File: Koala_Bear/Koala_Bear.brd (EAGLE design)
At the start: 59.3 x 40 mm, 28 parts

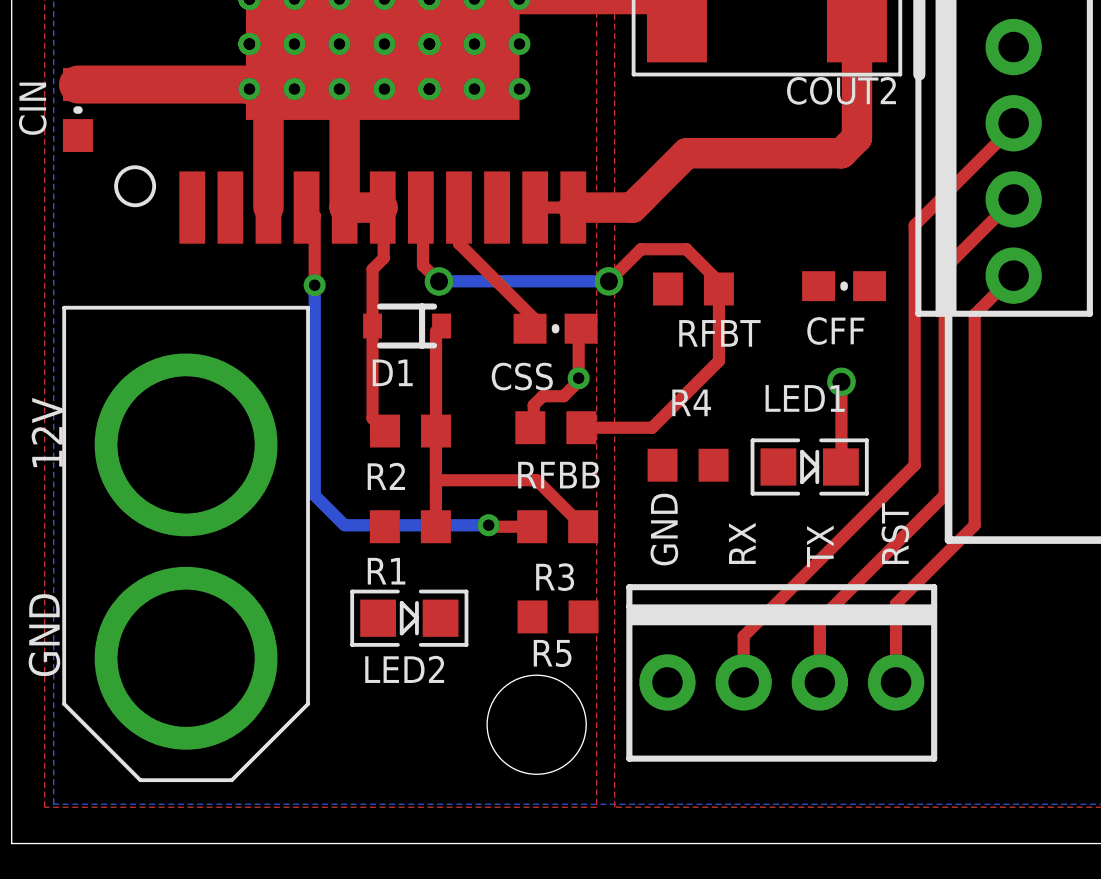
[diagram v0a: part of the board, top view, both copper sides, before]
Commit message: Rerouting completed
Koala should be successfully rerouted for RevB pending review.
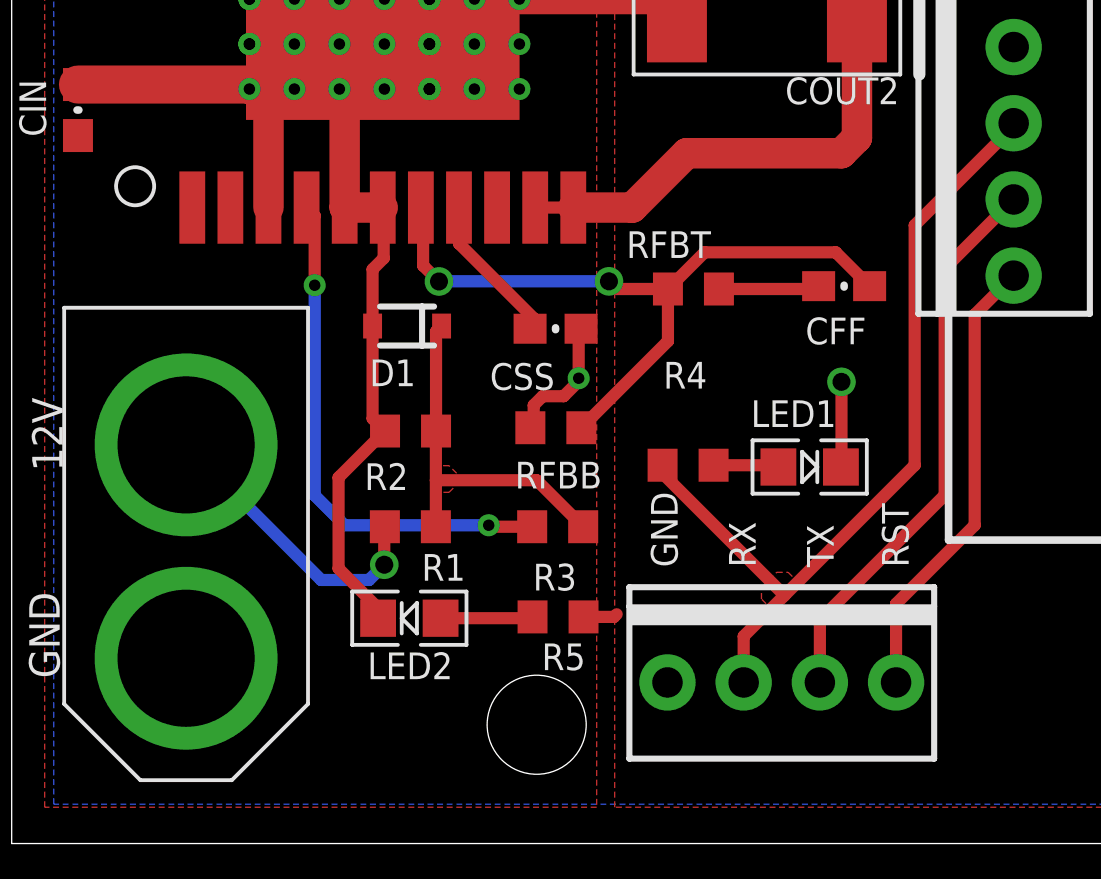
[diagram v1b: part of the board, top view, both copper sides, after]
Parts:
- turned LED2 to 180 degrees
- turned R4 to 180 degrees
- turned R5 to 0 degrees
- turned RFBT to 0 degrees
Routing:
- net VIN: track 0.00 -> 9.97 mm, vias 0 -> 1
- net GND: track 54.5 -> 61.9 mm
- net RX: track 22.4 -> 28.4 mm
- net VOUT: track 16.3 -> 20.2 mm
- net N$5: track 0.00 -> 3.08 mm
- net FB: track 21.2 -> 24.0 mm
- net N$1: track 0.00 -> 2.19 mm
- added copper zone on layer 1, net DIODE
- added copper zone on layer 1, net RX

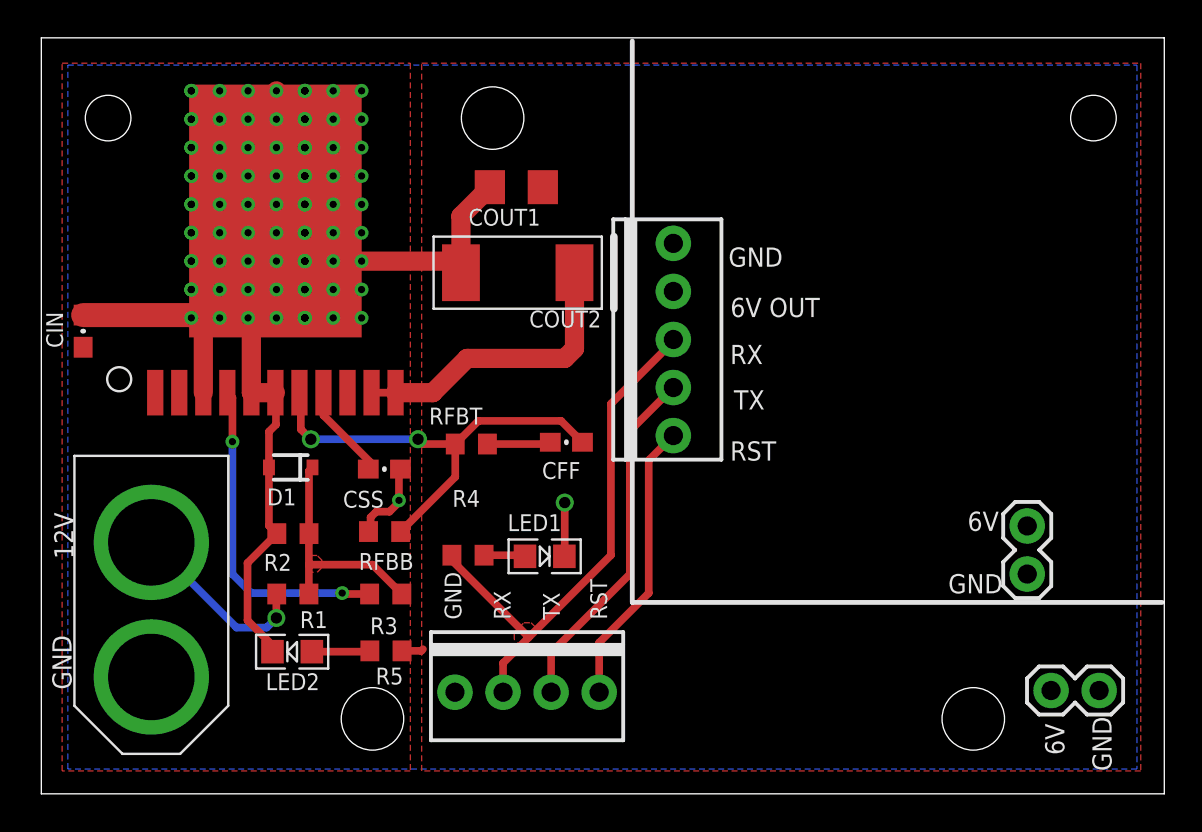
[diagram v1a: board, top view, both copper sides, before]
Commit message: Trying to negotiate hole clearances
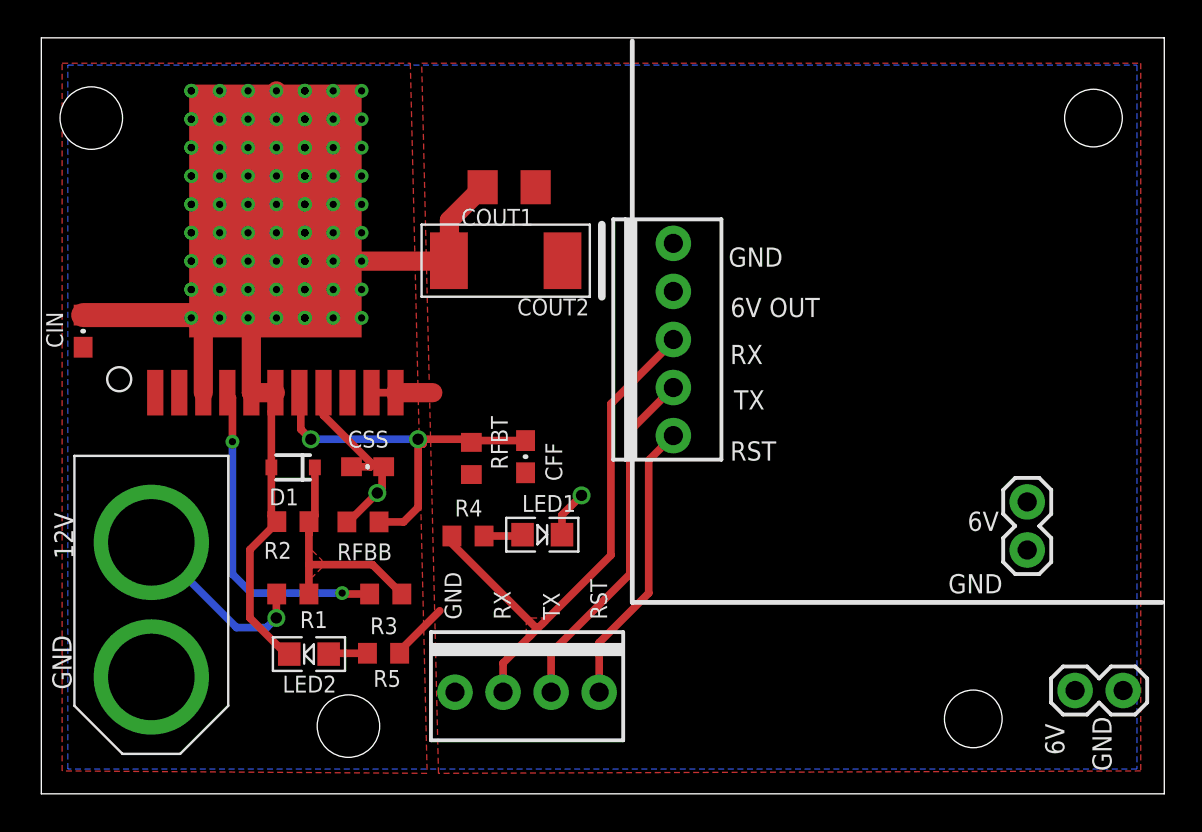
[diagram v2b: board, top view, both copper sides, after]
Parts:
- removed U$7, U$8: (no value), stand_off_servoc:STAND_OFF_SERVOC
- added U$2: (no value), pie:STAND-OFF-TIGHT
- MSTRO_PWR: value M05 -> (none)
- U$3: device SparkFun:STAND-OFF -> pie:STAND-OFF-TIGHT
- moved U$4 21.2 mm to (10.5, 38.1)
- moved CFF 2.29 mm to (33.5, 20.2), turned to 90 degrees
- moved U$5 1.33 mm to (24.1, 5.97)
- moved RFBB 1.25 mm to (24.9, 16.8)
- moved LED1 1.15 mm to (34.4, 16.1)
- moved R4 1.02 mm to (30.4, 16.0)
- moved CSS 0.90 mm to (25.1, 19.7)
- moved LED2 0.90 mm to (22.0, 9.77)
- moved COUT2 0.90 mm to (32.4, 30.6)
- moved RFBT 0.76 mm to (30.6, 20.1), turned to 270 degrees
- moved R2 0.63 mm to (21.2, 16.8)
- moved COUT1 0.38 mm to (32.6, 34.4)
- moved R5 0.18 mm to (26.0, 9.82)
- moved D1 0.13 mm to (21.2, 19.6)
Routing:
- net VOUT: track 20.2 -> 6.36 mm
- net FB: track 24.0 -> 20.9 mm
- net GND: track 61.9 -> 60.3 mm
- net N$5: track 3.08 -> 2.07 mm
- net SS: track 5.12 -> 5.96 mm
- net RX: track 28.4 -> 29.1 mm
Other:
- board text added: "PiE Robotics Buck Switching Regulator Version 2 : Revision B"
- board text removed: "PiE Robotics Buck Switching Regulator Version 2 : Revision A"

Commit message: Tentative RevB Submission
Changelog:

1. Have adjusted almost all hole positions, though I'm still a bit
worried about clearance. Feedback?
2. Changed LED1 from RX to TX so that it will actually work as intended
(blink when signal is being sent).
3. Made all routing changes suggested by Michael and Dennis (though the
LED trace change actually eliminated a need for one chamfer)

Things I'm worried about:
1. Clearance around the vReg, especially with the big capacitor.
Feedback?
2. Hole clearance
3. We made the decision to remove the holes in the uMaestro block that
would allow screws to be place through the maestro board into the
enclosure, and we also eliminated the holes that would allow a 12-pin
uMaestro to be attached. Do we want to scrap that functionality? The
stand-offs that Kate used in designing the board weren't from the PiE
library, and they aren't even in the standard Eagle library. Some of
them came from SparkFun and others came from a random "servoc" library.
Feedback?

Thanks!
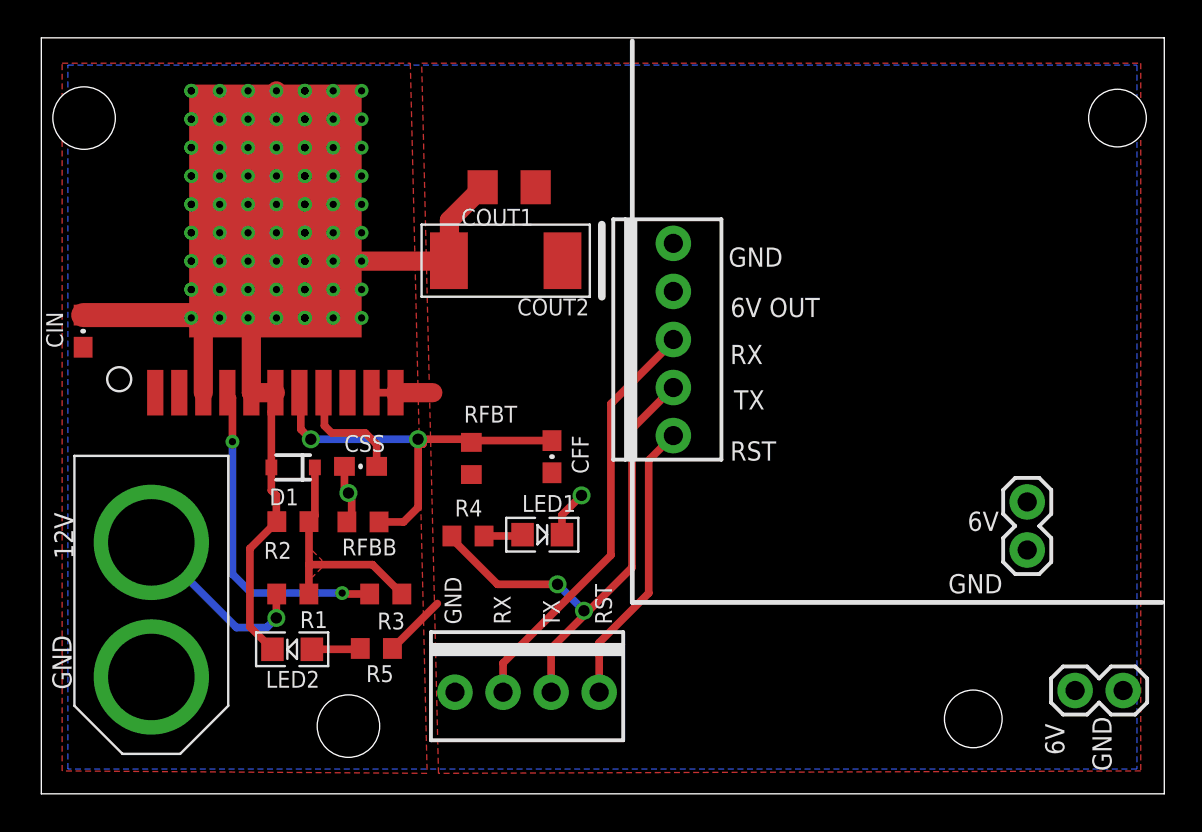
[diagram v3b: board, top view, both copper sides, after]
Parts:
- moved CFF 1.40 mm to (34.9, 20.2)
- moved U$2 1.27 mm to (64.8, 38.1)
- moved LED2 0.92 mm to (21.2, 10.0)
- moved R5 0.46 mm to (25.6, 10.1)
- moved U$4 0.38 mm to (10.2, 38.1)
- moved CSS 0.37 mm to (24.8, 19.7), turned to 180 degrees
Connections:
- net RX: no longer R4.2
- net TX: now also R4.2
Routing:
- net TX: track 18.8 -> 27.7 mm, vias 0 -> 2
- net RX: track 29.1 -> 22.4 mm
- net GND: track 60.3 -> 58.8 mm
- net FB: track 20.9 -> 22.3 mm
- net N$5: track 2.07 -> 2.58 mm
- removed copper zone on layer 1, net RX
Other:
- board text added: "100"
- board text added: "15.4k"
- board text added: "2.37k"
- board text added: "30k"
- board text added: "60k"

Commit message: Review fixes
I believe it should all be fixed now. All the capacitors have values and
all name/value positions are standardized (with the exception of COUT2
which hadn't sufficient room around the sides to place text.) Grizzly's
solution, while elegant, I don't think works as well here because we
don't have a bunch of components with the same value next to each other
as Grizzly does. Is there a way I can still do that here and clean up
the silkscreen?

In terms of the holes, I simply opted to move the hole in question to
the middle of the board to obviate the problem of the switching
regulator overlap altogether. Also, the holes at the bottom are at the
same height. Will enclosures people kill me for putting the holes at
.235 inches from the bottom of the board? I think the top-right mounting
hole actually misses the uMaestro altogether (the board was built to
accommodate a larger Maestro) and can go straight through into the
board. I hope. We'll have to test it.
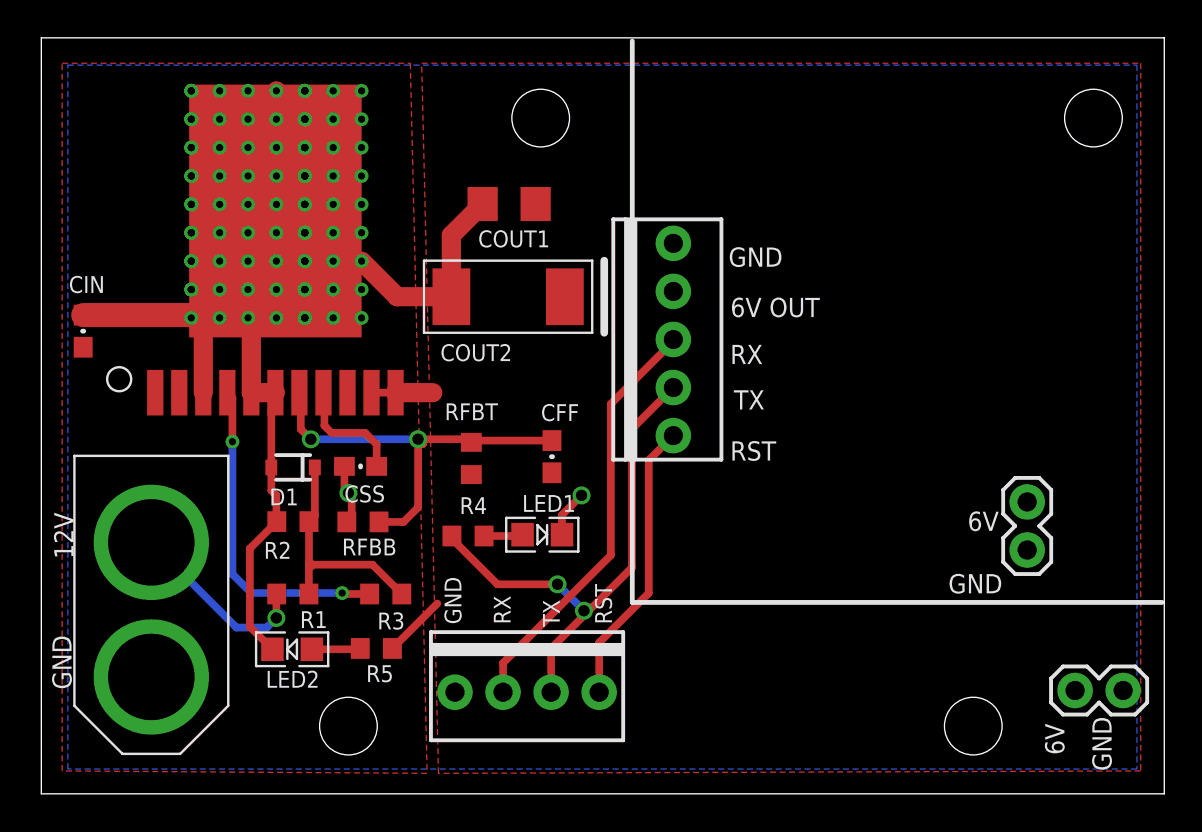
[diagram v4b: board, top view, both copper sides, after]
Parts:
- U$4, U$5: device SparkFun:STAND-OFF -> pie:STAND-OFF-TIGHT
- moved U$4 24.1 mm to (34.3, 38.1)
- moved COUT2 1.91 mm to (32.6, 28.7)
- moved U$2 1.27 mm to (63.5, 38.1)
- moved COUT1 0.89 mm to (32.6, 33.6)
- moved U$3 0.38 mm to (57.1, 5.97)
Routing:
- net GND: track 58.8 -> 60.6 mm
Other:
- board text added: ".47uf"
- board text added: "10uf"
- board text added: "4.7n"
- board text added: "470uf"
- board text added: "47uf"
- board text added: "5.1V"
